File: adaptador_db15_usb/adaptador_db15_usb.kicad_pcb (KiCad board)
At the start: 2 copper layers, 100 x 100 mm, 26 parts, among them J1 Conn_01x34, J2 A-USB3_A-LP-SMT1, J3 A-USB3_A-LP-SMT1

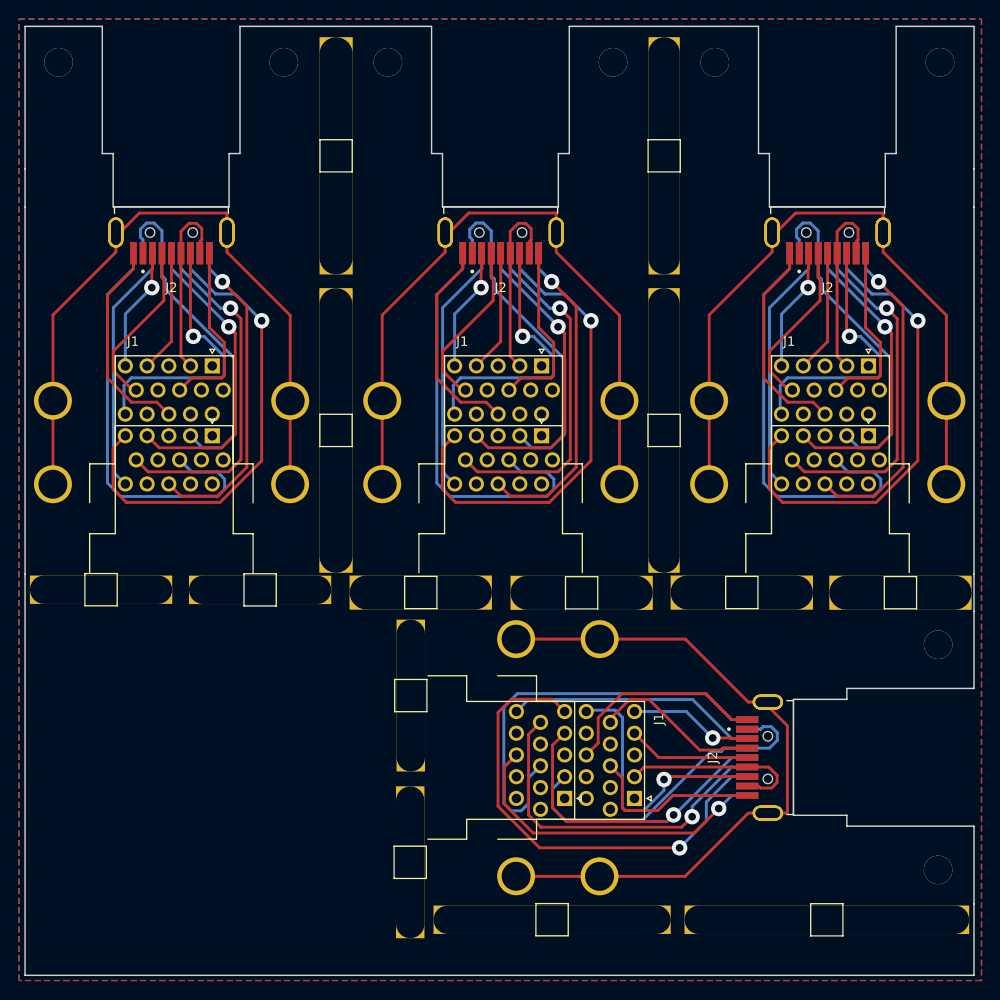
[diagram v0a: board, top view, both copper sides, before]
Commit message: New PCB of the Adapter
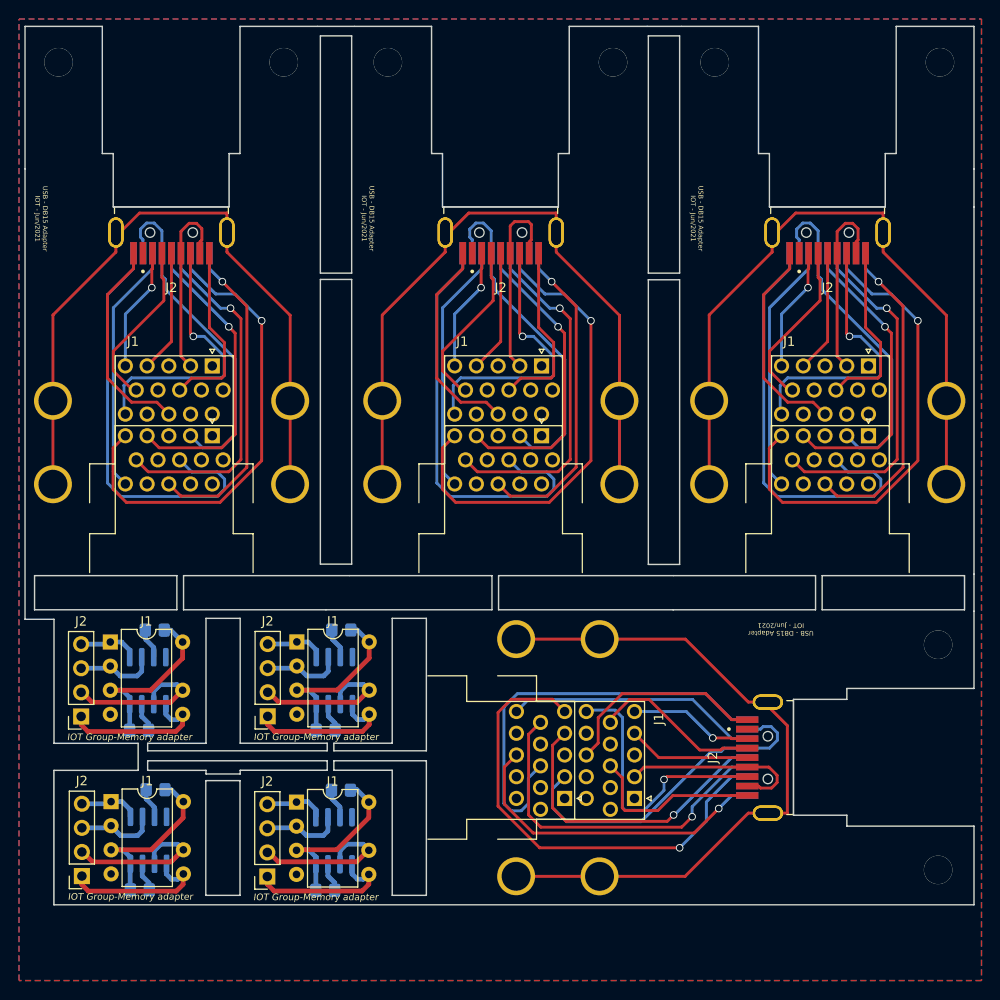
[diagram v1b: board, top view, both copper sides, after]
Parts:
- removed REF** (x14): TestPoint_THTPad_3.0x3.0mm_Drill1.5mm, TestPoint:TestPoint_THTPad_3.0x3.0mm_Drill1.5mm
- added J1: Conn_01x08_Female, Package_DIP:DIP-8-N7_W7.62mm, F.Cu at (119.3, 122.7)
- added J1: Conn_01x08_Female, Package_DIP:DIP-8-N7_W7.62mm, F.Cu at (119.3, 105.9)
- added J1: Conn_01x08_Female, Package_DIP:DIP-8-N7_W7.62mm, F.Cu at (138.9, 105.9)
- added J1: Conn_01x08_Female, Package_DIP:DIP-8-N7_W7.62mm, F.Cu at (138.9, 122.8)
- added J2: Conn_01x04_Male, Connector_PinSocket_2.54mm:PinSocket_1x04_P2.54mm_Vertical, F.Cu at (116.3, 130.6)
- added J2: Conn_01x04_Male, Connector_PinSocket_2.54mm:PinSocket_1x04_P2.54mm_Vertical, F.Cu at (116.2, 113.7)
- added J2: Conn_01x04_Male, Connector_PinSocket_2.54mm:PinSocket_1x04_P2.54mm_Vertical, F.Cu at (135.8, 113.7)
- added J2: Conn_01x04_Male, Connector_PinSocket_2.54mm:PinSocket_1x04_P2.54mm_Vertical, F.Cu at (135.8, 130.6)
- added R1: R, Resistor_SMD:R_0805_2012Metric_Pad1.20x1.40mm_HandSolder, B.Cu at (124.0, 121.5)
- added R1: R, Resistor_SMD:R_0805_2012Metric_Pad1.20x1.40mm_HandSolder, B.Cu at (123.9, 104.6)
- added R1: R, Resistor_SMD:R_0805_2012Metric_Pad1.20x1.40mm_HandSolder, B.Cu at (143.6, 104.6)
- added R1: R, Resistor_SMD:R_0805_2012Metric_Pad1.20x1.40mm_HandSolder, B.Cu at (143.6, 121.5)
- added R2: R, Resistor_SMD:R_0805_2012Metric_Pad1.20x1.40mm_HandSolder, B.Cu at (122.4, 132.0)
- added R2: R, Resistor_SMD:R_0805_2012Metric_Pad1.20x1.40mm_HandSolder, B.Cu at (122.3, 115.2)
- added R2: R, Resistor_SMD:R_0805_2012Metric_Pad1.20x1.40mm_HandSolder, B.Cu at (141.9, 115.2)
- added R2: R, Resistor_SMD:R_0805_2012Metric_Pad1.20x1.40mm_HandSolder, B.Cu at (141.9, 132.1)
- added U1: M95XXX, Package_SO:SOIC-8_3.9x4.9mm_P1.27mm, B.Cu at (123.3, 126.8)
- added U1: M95XXX, Package_SO:SOIC-8_3.9x4.9mm_P1.27mm, B.Cu at (123.2, 110.0)
- added U1: M95XXX, Package_SO:SOIC-8_3.9x4.9mm_P1.27mm, B.Cu at (142.9, 110.0)
- added U1: M95XXX, Package_SO:SOIC-8_3.9x4.9mm_P1.27mm, B.Cu at (142.8, 126.8)
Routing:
- net /5v: track 0.00 -> 77.8 mm
- net /Mosi: track 0.00 -> 66.3 mm
- net /clk: track 0.00 -> 65.7 mm
- net /miso: track 0.00 -> 34.4 mm
- net /cs: track 0.00 -> 25.2 mm
- net Net-(R1-Pad1): track 0.00 -> 12.9 mm
- net Net-(R2-Pad1): track 0.00 -> 12.2 mm
- net /0v1: track 80.2 -> 81.0 mm
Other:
- board size 100 x 100 mm -> 100 x 92.6 mm
- net class Default: clearance 0.3048 -> 0.2; trace_width 0.3048 -> 0.25; via_dia 1.6256 -> 0.8; via_drill 0.8128 -> 0.4
- rule pad_to_mask_clearance: 0.051 -> 0
- rule trace_clearance: 0.3048 -> 0.2
- board text added: "Cut Inside"
- board text added: "IOT Group-Memory adapter"
- board text added: "USB - DB15 Adapter IOT - Jun/2021"
- board text added: "~S~ Q C D"
